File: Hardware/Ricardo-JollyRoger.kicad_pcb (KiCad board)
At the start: 4 copper layers, 45.8 x 35.8 mm, 88 parts, among them J1 RBUS, J2 USB_C_Receptacle_USB2.0, J3 Conn_01x08_Pin, J4 Conn_01x06_Pin, U1 ESP32-S3, U2 SN65HVD230, U3 LM66200DRLR, U4 MAX77827AEFD+T, U5 SC4215ASTRT, U7 LM66200DRLR, U8 ZDSD04GLGEAG, Y1 R940000171

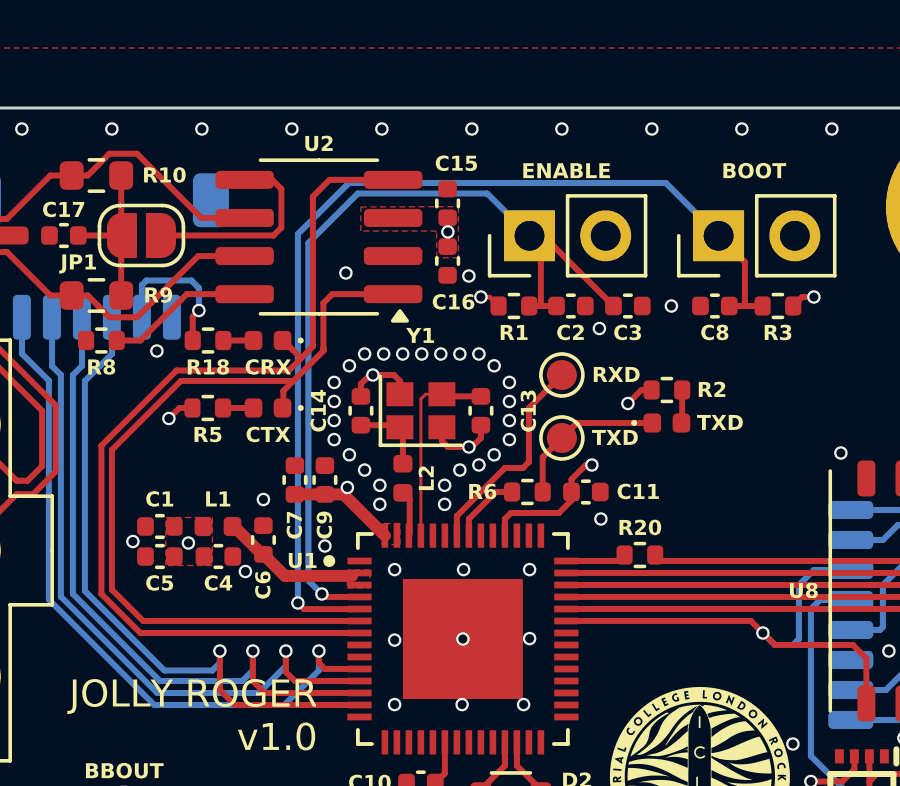
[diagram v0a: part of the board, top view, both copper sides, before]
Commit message: Moved 3V3 via
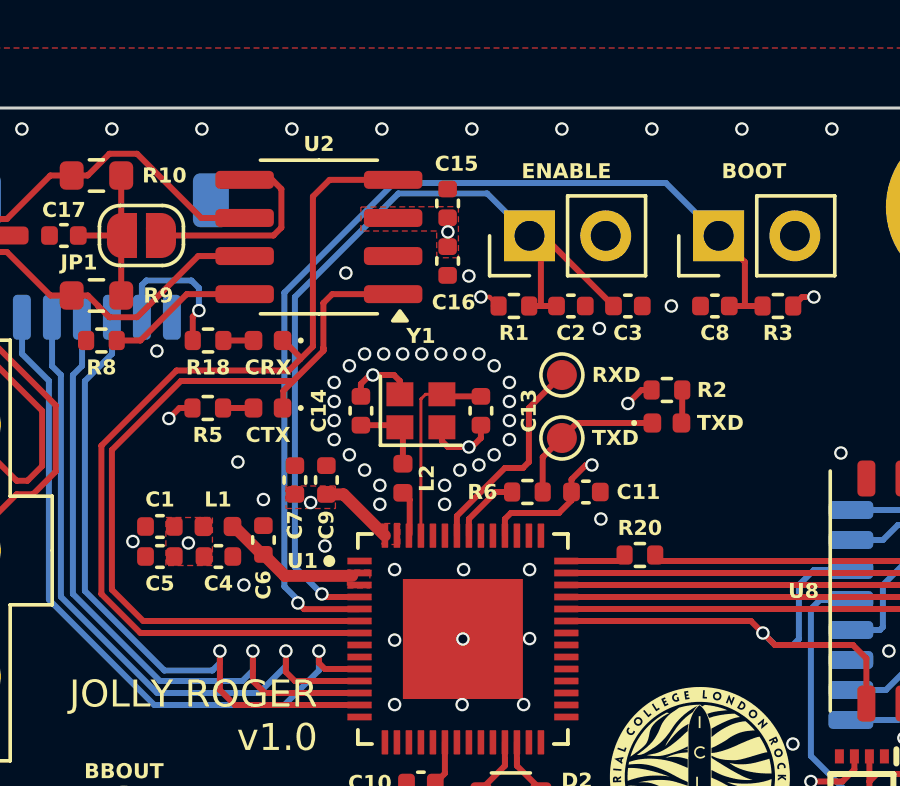
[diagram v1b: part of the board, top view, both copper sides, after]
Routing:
- net +3V3: track 28.5 -> 27.5 mm
- net /BOOT: track 33.7 -> 33.2 mm
- net GND: vias 108 -> 109
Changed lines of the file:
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@@
 	(footprint "Capacitor_SMD:C_0402_1005Metric"
 		(layer "F.Cu")
-		(at 100.125 57.49 90)
+		(at 100.175 57.49 90)
 		(descr "Capacitor SMD 0402 (1005 Metric), square (rectangular) end terminal, IPC_7351 nominal, (Body size source: IPC-SM-782 page 76, https://www.pcb-3d.com/wordpress/wp-content/uploads/ipc-sm-782a_amendment_1_and_2.pdf), generated with kicad-footprint-generator")
 		(tags "capacitor")
@@
 	)
 	(via
-		(at 97.475 60.54)
+		(at 97.425 60.99)
 		(size 0.45)
 		(drill 0.3)
@@
 	)
 	(via
+		(at 97.225 56.89)
+		(size 0.45)
+		(drill 0.3)
+		(layers "F.Cu" "B.Cu")
+		(free yes)
+		(net 1)
+	)
+	(via
 		(at 79.825 53.99)
 		(size 0.45)
@@
 	)
 	(segment
-		(start 99.125 57.97)
-		(end 100.125 57.97)
-		(width 0.4)
-		(layer "F.Cu")
-		(net 2)
-	)
-	(segment
 		(start 117.3745 67.54)
 		(end 117.775 67.1395)
@@
 	)
 	(via
-		(at 100.875 57.74)
-		(size 0.45)
-		(drill 0.3)
-		(layers "F.Cu" "B.Cu")
-		(free yes)
-		(net 2)
-	)
-	(via
 		(at 110.225 54.94)
 		(size 0.45)
@@
 	)
 	(via
+		(at 99.65 58.24)
+		(size 0.45)
+		(drill 0.3)
+		(layers "F.Cu" "B.Cu")
+		(free yes)
+		(net 2)
+	)
+	(via
 		(at 84.165 71.69)
 		(size 0.45)
@@
 	)
 	(segment
-		(start 111.49 47.59)
-		(end 113.25 49.35)
+		(start 102.430025 47.59)
+		(end 111.49 47.59)
+		(width 0.2)
+		(layer "B.Cu")
+		(net 20)
+	)
+	(segment
+		(start 98.775 51.245025)
+		(end 102.430025 47.59)
 		(width 0.2)
 		(layer "B.Cu")
@@
 	(segment
 		(start 99.225 61.59)
-		(end 99.225 49.29)
+		(end 99.225 61.49)
 		(width 0.2)
 		(layer "B.Cu")
@@
 	)
 	(segment
-		(start 99.225 49.29)
-		(end 100.925 47.59)
+		(start 111.49 47.59)
+		(end 113.25 49.35)
 		(width 0.2)
 		(layer "B.Cu")
@@
 	)
 	(segment
-		(start 100.925 47.59)
-		(end 111.49 47.59)
+		(start 99.225 61.49)
+		(end 98.775 61.04)
+		(width 0.2)
+		(layer "B.Cu")
+		(net 20)
+	)
+	(segment
+		(start 98.775 61.04)
+		(end 98.775 51.245025)
 		(width 0.2)
 		(layer "B.Cu")
@@
 	)
 	(segment
-		(start 99.575 60.84)
-		(end 99.575 49.59)
+		(start 99.125 60.39)
+		(end 99.125 51.39)
 		(width 0.2)
 		(layer "B.Cu")
@@
 	)
 	(segment
-		(start 100.025 61.29)
-		(end 99.575 60.84)
+		(start 105.535 47.94)
+		(end 106.945 49.35)
 		(width 0.2)
 		(layer "B.Cu")
@@
 	)
 	(segment
-		(start 99.575 49.59)
-		(end 101.225 47.94)
+		(start 102.575 47.94)
+		(end 105.535 47.94)
 		(width 0.2)
 		(layer "B.Cu")
@@
 	)
 	(segment
-		(start 105.535 47.94)
-		(end 106.945 49.35)
+		(start 100.025 61.29)
+		(end 99.125 60.39)
 		(width 0.2)
 		(layer "B.Cu")
@@
 	)
 	(segment
-		(start 101.225 47.94)
-		(end 105.535 47.94)
+		(start 99.125 51.39)
+		(end 102.575 47.94)
 		(width 0.2)
 		(layer "B.Cu")
@@
 	)
 	(zone
-		(net 1)
-		(net_name "GND")
-		(layer "F.Cu")
-		(name "$teardrop_padvia$")
-		(hatch full 0.1)
-		(priority 30002)
-		(attr
-			(teardrop
-				(type padvia)
-			)
-		)
-		(connect_pads yes
-			(clearance 0)
-		)
-		(min_thickness 0.0254)
-		(filled_areas_thickness no)
-		(fill yes
-			(thermal_gap 0.5)
-			(thermal_bridge_width 0.5)
-			(island_removal_mode 1)
-			(island_area_min 10)
-		)
-		(polygon
-			(pts
-				(xy 88.316888 72.386882) (xy 88.566888 72.386882) (xy 88.649761 72.022986) (xy 88.441888 71.935882)
-				(xy 88.234015 72.022986)
-			)
-		)
-	)
-	(zone
 		(net 5)
 		(net_name "/Power/BBIN")
@@
 	)
 	(zone
-		(net 3)
-		(net_name "VBUS")
-		(layer "F.Cu")
-		(name "$teardrop_padvia$")
-		(hatch full 0.1)
-		(priority 30001)
-		(attr
-			(teardrop
-				(type padvia)
-			)
-		)
-		(connect_pads yes
-			(clearance 0)
-		)
-		(min_thickness 0.0254)
-		(filled_areas_thickness no)
-		(fill yes
-			(thermal_gap 0.5)
-			(thermal_bridge_width 0.5)
-			(island_removal_mode 1)
-			(island_area_min 10)
-		)
-		(polygon
-			(pts
-				(xy 88.274825 76.3) (xy 88.274825 75.9) (xy 88.065987 75.742783) (xy 87.905888 75.901882) (xy 87.820784 76.109755)
-			)
-		)
-	)
-	(zone
 		(net 2)
 		(net_name "+3V3")
@@
 	)
 	(zone
+		(net 1)
+		(net_name "GND")
+		(layer "F.Cu")
+		(name "$teardrop_padvia$")
+		(hatch full 0.1)
+		(priority 30002)
+		(attr
+			(teardrop
+				(type padvia)
+			)
+		)
+		(connect_pads yes
+			(clearance 0)
+		)
+		(min_thickness 0.0254)
+		(filled_areas_thickness no)
+		(fill yes
+			(thermal_gap 0.5)
+			(thermal_bridge_width 0.5)
+			(island_removal_mode 1)
+			(island_area_min 10)
+		)
+		(polygon
+			(pts
+				(xy 88.316888 72.386882) (xy 88.566888 72.386882) (xy 88.649761 72.022986) (xy 88.441888 71.935882)
+				(xy 88.234015 72.022986)
+			)
+		)
+	)
+	(zone
 		(net 8)
 		(net_name "/Power/LX1")
@@
 	)
 	(zone
+		(net 3)
+		(net_name "VBUS")
+		(layer "F.Cu")
+		(name "$teardrop_padvia$")
+		(hatch full 0.1)
+		(priority 30001)
+		(attr
+			(teardrop
+				(type padvia)
+			)
+		)
+		(connect_pads yes
+			(clearance 0)
+		)
+		(min_thickness 0.0254)
+		(filled_areas_thickness no)
+		(fill yes
+			(thermal_gap 0.5)
+			(thermal_bridge_width 0.5)
+			(island_removal_mode 1)
+			(island_area_min 10)
+		)
+		(polygon
+			(pts
+				(xy 88.274825 76.3) (xy 88.274825 75.9) (xy 88.065987 75.742783) (xy 87.905888 75.901882) (xy 87.820784 76.109755)
+			)
+		)
+	)
+	(zone
 		(net 8)
 		(net_name "/Power/LX1")
@@
 	)
 	(zone
+		(net 2)
+		(net_name "+3V3")
+		(layer "F.Cu")
+		(hatch edge 0.5)
+		(priority 7)
+		(connect_pads yes
+			(clearance 0)
+		)
+		(min_thickness 0.25)
+		(filled_areas_thickness no)
+		(fill yes
+			(thermal_gap 0.5)
+			(thermal_bridge_width 0.5)
+		)
+		(polygon
+			(pts
+				(xy 98.825 58.44) (xy 100.475 58.44) (xy 100.475 57.69) (xy 98.825 57.69)
+			)
+		)
+	)
+	(zone
 		(net 0)
 		(net_name "")
@@
 		(name "$teardrop_padvia$")
 		(hatch full 0.1)
-		(priority 30000)
+		(priority 30001)
 		(attr
 			(teardrop
@@
 		(polygon
 			(pts
-				(xy 87.325 72.04) (xy 87.725 72.04) (xy 87.75 71.59) (xy 87.525 71.589) (xy 87.3 71.59)
+				(xy 87.984619 71.413224) (xy 87.701776 71.130381) (xy 87.365901 71.430901) (xy 87.524293 71.590707)
+				(xy 87.684099 71.749099)
 			)
 		)
@@
 	)
 	(zone
-		(net 3)
-		(net_name "VBUS")
+		(net 1)
+		(net_name "GND")
 		(layer "B.Cu")
-		(name "$teardrop_padvia$")
-		(hatch full 0.1)
-		(priority 30001)
-		(attr
-			(teardrop
-				(type padvia)
-			)
-		)
+		(hatch edge 0.5)
+		(priority 1)
 		(connect_pads yes
 			(clearance 0)
 		)
-		(min_thickness 0.0254)
+		(min_thickness 0.25)
 		(filled_areas_thickness no)
 		(fill yes
 			(thermal_gap 0.5)
 			(thermal_bridge_width 0.5)
-			(island_removal_mode 1)
-			(island_area_min 10)
 		)
 		(polygon
 			(pts
-				(xy 87.984619 71.413224) (xy 87.701776 71.130381) (xy 87.365901 71.430901) (xy 87.524293 71.590707)
-				(xy 87.684099 71.749099)
+				(xy 135.925 35.59) (xy 135.925 90.59) (xy 65.925 90.59) (xy 65.925 35.59)
 			)
 		)
 	)
 	(zone
-		(net 1)
-		(net_name "GND")
+		(net 3)
+		(net_name "VBUS")
 		(layer "B.Cu")
-		(hatch edge 0.5)
-		(priority 1)
+		(name "$teardrop_padvia$")
+		(hatch full 0.1)
+		(priority 30002)
+		(attr
+			(teardrop
+				(type padvia)
+			)
+		)
 		(connect_pads yes
 			(clearance 0)
 		)
-		(min_thickness 0.25)
+		(min_thickness 0.0254)
 		(filled_areas_thickness no)
 		(fill yes
 			(thermal_gap 0.5)
 			(thermal_bridge_width 0.5)
+			(island_removal_mode 1)
+			(island_area_min 10)
 		)
 		(polygon
 			(pts
-				(xy 135.925 35.59) (xy 135.925 90.59) (xy 65.925 90.59) (xy 65.925 35.59)
+				(xy 87.730112 75.442263) (xy 87.447269 75.725106) (xy 87.747789 76.060981) (xy 87.907595 75.902589)
+				(xy 88.065987 75.742783)
 			)
 		)
@@
 		(name "$teardrop_padvia$")
 		(hatch full 0.1)
-		(priority 30002)
+		(priority 30000)
 		(attr
 			(teardrop
@@
 		(polygon
 			(pts
-				(xy 87.730112 75.442263) (xy 87.447269 75.725106) (xy 87.747789 76.060981) (xy 87.907595 75.902589)
-				(xy 88.065987 75.742783)
+				(xy 87.325 72.04) (xy 87.725 72.04) (xy 87.75 71.59) (xy 87.525 71.589) (xy 87.3 71.59)
 			)
 		)

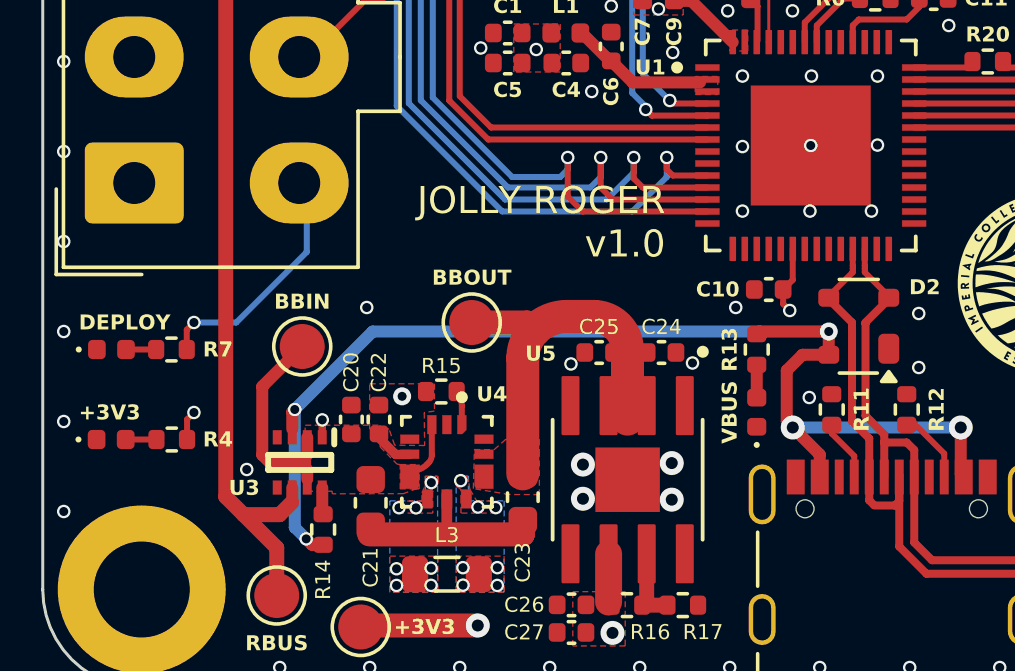
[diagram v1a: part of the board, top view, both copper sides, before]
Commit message: Added barcode square
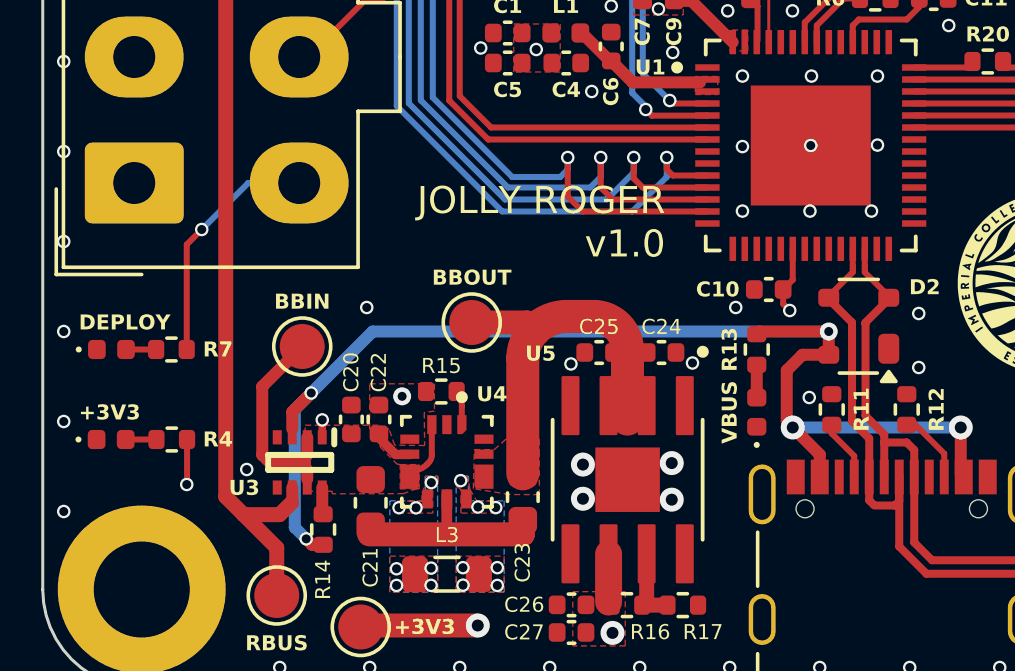
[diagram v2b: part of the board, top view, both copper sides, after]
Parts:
- moved G*** 2.06 mm to (91.9, 76.6)
- moved G*** 1.58 mm to (98.4, 76.6)
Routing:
- net VBUS: track 41.1 -> 41.9 mm
- net +3V3: track 27.5 -> 28.0 mm
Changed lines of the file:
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@@
 	(footprint "iclr:iclr_logo_estd2018_6mm"
 		(layer "B.Cu")
-		(at 89.925 76.09 180)
+		(at 91.925 76.59 180)
 		(property "Reference" "G***"
 			(at 0 0 0)
@@
 	(footprint "iclr:rae_logo_6mm"
 		(layer "B.Cu")
-		(at 96.925 76.09 180)
+		(at 98.425 76.59 180)
 		(property "Reference" "G***"
 			(at 0 0 0)
@@
 		)
 	)
+	(gr_rect
+		(start 82.425 66.59)
+		(end 87.425 71.59)
+		(stroke
+			(width 0.15)
+			(type solid)
+		)
+		(fill solid)
+		(layer "B.SilkS")
+	)
 	(gr_arc
 		(start 79.125 48.39)
@@
 	)
 	(gr_text "{dblquote}Not all treasure is silver and gold, mate{dblquote}"
-		(at 117.675 76.84 0)
+		(at 118.425 76.84 0)
 		(layer "B.SilkS")
 		(effects
@@
 	)
 	(segment
+		(start 83.935 74.08)
+		(end 83.935 72.59)
+		(width 0.2)
+		(layer "F.Cu")
+		(net 2)
+	)
+	(segment
 		(start 116.035 51.39)
 		(end 115.735 51.69)
@@
 	)
 	(segment
-		(start 84.165 71.69)
-		(end 83.935 71.92)
-		(width 0.2)
-		(layer "F.Cu")
-		(net 2)
-	)
-	(segment
 		(start 93.625 78.79)
 		(end 89.775 78.79)
@@
 	)
 	(segment
-		(start 83.935 71.92)
-		(end 83.935 72.59)
-		(width 0.2)
-		(layer "F.Cu")
-		(net 2)
-	)
-	(segment
 		(start 108.825 56.99)
 		(end 108.345 57.47)
@@
 		(net 2)
 	)
+	(segment
+		(start 83.925 74.09)
+		(end 83.935 74.08)
+		(width 0.2)
+		(layer "F.Cu")
+		(net 2)
+	)
 	(via
 		(at 110.225 54.94)
@@
 	)
 	(via
-		(at 84.165 71.69)
+		(at 83.925 74.09)
 		(size 0.45)
 		(drill 0.3)
@@
 	)
 	(segment
-		(start 87.525 71.59)
-		(end 87.441888 71.673112)
-		(width 0.4)
-		(layer "F.Cu")
-		(net 3)
-	)
-	(segment
 		(start 103.925 70.29)
 		(end 104.45 69.765)
@@
 	)
 	(segment
-		(start 87.441888 71.673112)
-		(end 87.441888 72.238065)
+		(start 88.075 71.04)
+		(end 87.441888 71.673112)
 		(width 0.4)
 		(layer "F.Cu")
@@
 	)
 	(segment
+		(start 87.441888 71.673112)
+		(end 87.441888 72.238065)
+		(width 0.4)
+		(layer "F.Cu")
+		(net 3)
+	)
+	(segment
 		(start 88.471888 76.1)
 		(end 88.529888 76.042)
@@
 	)
 	(via
-		(at 87.525 71.59)
+		(at 88.075 71.04)
 		(size 0.45)
 		(drill 0.3)
@@
 	)
 	(segment
-		(start 105.325 68.99)
-		(end 90.125 68.99)
+		(start 90.125 68.99)
+		(end 105.325 68.99)
 		(width 0.4)
 		(layer "B.Cu")
@@
 	)
 	(segment
-		(start 90.125 68.99)
+		(start 87.525 71.59)
+		(end 87.525 75.519994)
+		(width 0.4)
+		(layer "B.Cu")
+		(net 3)
+	)
+	(segment
+		(start 88.075 71.04)
 		(end 87.525 71.59)
 		(width 0.4)
@@
 	)
 	(segment
-		(start 87.525 75.519994)
-		(end 87.906888 75.901882)
+		(start 88.075 71.04)
+		(end 90.125 68.99)
 		(width 0.4)
 		(layer "B.Cu")
@@
 	)
 	(segment
-		(start 87.525 71.59)
-		(end 87.525 75.519994)
+		(start 87.525 75.519994)
+		(end 87.906888 75.901882)
 		(width 0.4)
 		(layer "B.Cu")
@@
 	)
 	(segment
-		(start 84.165 68.69)
-		(end 83.925 68.93)
+		(start 83.925 66.09)
+		(end 83.925 69.59)
 		(width 0.2)
 		(layer "F.Cu")
@@
 	)
 	(segment
-		(start 83.925 68.93)
-		(end 83.925 69.59)
+		(start 84.425 65.59)
+		(end 83.925 66.09)
 		(width 0.2)
 		(layer "F.Cu")
@@
 	)
 	(via
-		(at 84.165 68.69)
+		(at 84.425 65.59)
 		(size 0.45)
 		(drill 0.3)
@@
 	)
 	(segment
-		(start 87.925 66.34)
-		(end 87.925 64.04)
+		(start 85.975 64.04)
+		(end 87.425 64.04)
 		(width 0.2)
 		(layer "B.Cu")
@@
 	)
 	(segment
-		(start 85.575 68.69)
-		(end 87.925 66.34)
+		(start 84.425 65.59)
+		(end 85.975 64.04)
 		(width 0.2)
 		(layer "B.Cu")
@@
 	)
 	(segment
-		(start 84.165 68.69)
-		(end 85.575 68.69)
+		(start 87.425 64.04)
+		(end 87.675 64.29)
 		(width 0.2)
 		(layer "B.Cu")
@@
 	)
 	(zone
-		(net 1)
-		(net_name "GND")
-		(layer "F.Cu")
-		(name "$teardrop_padvia$")
-		(hatch full 0.1)
-		(priority 30002)
-		(attr
-			(teardrop
-				(type padvia)
-			)
-		)
-		(connect_pads yes
-			(clearance 0)
-		)
-		(min_thickness 0.0254)
-		(filled_areas_thickness no)
-		(fill yes
-			(thermal_gap 0.5)
-			(thermal_bridge_width 0.5)
-			(island_removal_mode 1)
-			(island_area_min 10)
-		)
-		(polygon
-			(pts
-				(xy 88.316888 72.386882) (xy 88.566888 72.386882) (xy 88.649761 72.022986) (xy 88.441888 71.935882)
-				(xy 88.234015 72.022986)
-			)
-		)
-	)
-	(zone
 		(net 8)
 		(net_name "/Power/LX1")
@@
 		(polygon
 			(pts
-				(xy 87.241888 72.023468) (xy 87.641888 72.023468) (xy 87.732873 71.676104) (xy 87.525 71.589) (xy 87.3 71.59)
+				(xy 87.615381 71.216776) (xy 87.898224 71.499619) (xy 88.234099 71.199099) (xy 88.075707 71.039293)
+				(xy 87.915901 70.880901)
 			)
 		)
@@
 	)
 	(zone
+		(net 1)
+		(net_name "GND")
+		(layer "F.Cu")
+		(name "$teardrop_padvia$")
+		(hatch full 0.1)
+		(priority 30002)
+		(attr
+			(teardrop
+				(type padvia)
+			)
+		)
+		(connect_pads yes
+			(clearance 0)
+		)
+		(min_thickness 0.0254)
+		(filled_areas_thickness no)
+		(fill yes
+			(thermal_gap 0.5)
+			(thermal_bridge_width 0.5)
+			(island_removal_mode 1)
+			(island_area_min 10)
+		)
+		(polygon
+			(pts
+				(xy 88.316888 72.386882) (xy 88.566888 72.386882) (xy 88.649761 72.022986) (xy 88.441888 71.935882)
+				(xy 88.234015 72.022986)
+			)
+		)
+	)
+	(zone
 		(net 2)
 		(net_name "+3V3")
@@
 		(name "$teardrop_padvia$")
 		(hatch full 0.1)
-		(priority 30001)
+		(priority 30000)
 		(attr
 			(teardrop
@@
 		(polygon
 			(pts
-				(xy 87.984619 71.413224) (xy 87.701776 71.130381) (xy 87.365901 71.430901) (xy 87.524293 71.590707)
-				(xy 87.684099 71.749099)
+				(xy 88.534619 70.863224) (xy 88.251776 70.580381) (xy 87.915901 70.880901) (xy 88.074293 71.040707)
+				(xy 88.234099 71.199099)
 			)
 		)
@@
 		(polygon
 			(pts
-				(xy 87.730112 75.442263) (xy 87.447269 75.725106) (xy 87.747789 76.060981) (xy 87.907595 75.902589)
-				(xy 88.065987 75.742783)
+				(xy 87.615381 71.216776) (xy 87.898224 71.499619) (xy 88.234099 71.199099) (xy 88.075707 71.039293)
+				(xy 87.915901 70.880901)
 			)
 		)
@@
 		(name "$teardrop_padvia$")
 		(hatch full 0.1)
-		(priority 30000)
+		(priority 30001)
 		(attr
 			(teardrop
@@
 		(polygon
 			(pts
-				(xy 87.325 72.04) (xy 87.725 72.04) (xy 87.75 71.59) (xy 87.525 71.589) (xy 87.3 71.59)
+				(xy 87.730112 75.442263) (xy 87.447269 75.725106) (xy 87.747789 76.060981) (xy 87.907595 75.902589)
+				(xy 88.065987 75.742783)
 			)
 		)
